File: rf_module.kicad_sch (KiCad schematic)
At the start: 23 parts, among them J5 RF Antenna, Q1 BC848, Q2 BC848, U7 SIM800C-DS

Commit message: Dual SIM version
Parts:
- removed Q1, Q2: BC848, Package_TO_SOT_SMD:SOT-23, symbol Transistor_BJT:BC848
- removed R15, R19: 4.7k, Resistor_SMD:R_0805_2012Metric_Pad1.20x1.40mm_HandSolder, symbol Device:R
- removed R16, R20: 47k, Resistor_SMD:R_0805_2012Metric_Pad1.20x1.40mm_HandSolder, symbol Device:R
- added Q1: MUN5233DW1, Package_TO_SOT_SMD:SOT-363_SC-70-6, symbol symbols:MUN5233DW1
- renumbered R17 to R15, R18 to R16, R21 to R17
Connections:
- net GNDD: now also Q1.1 (E), Q1.4 (E)
- net NETLIGHT: now also Q1.5 (B)
- net STATUS: now also Q1.2 (B)
- net at D6.1 (K): now also Q1.6 (C)
- net at D8.1 (K): now also Q1.3 (C)

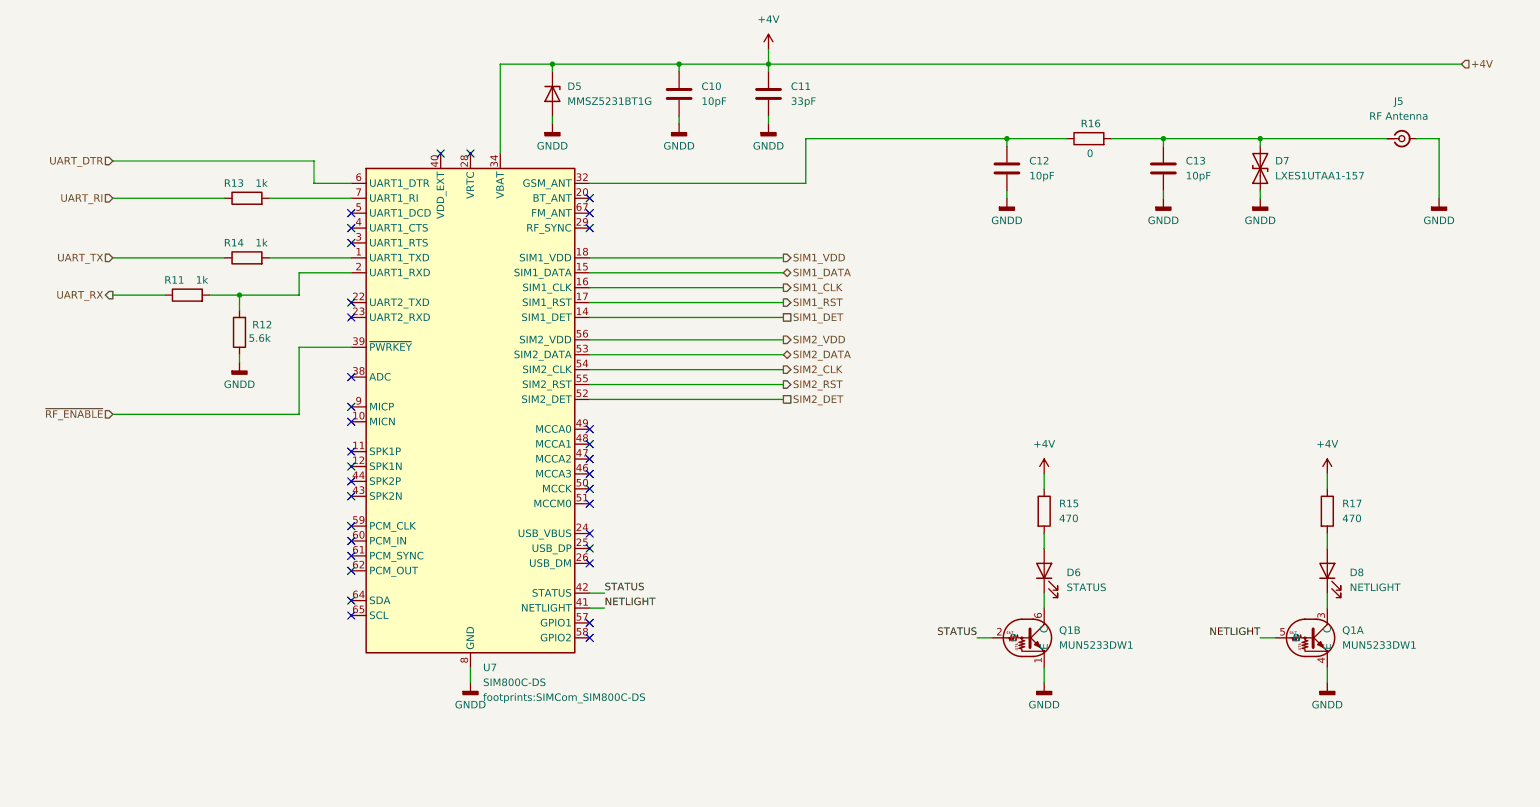
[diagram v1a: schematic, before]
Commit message: Replace SIM800C-DS with A7682E
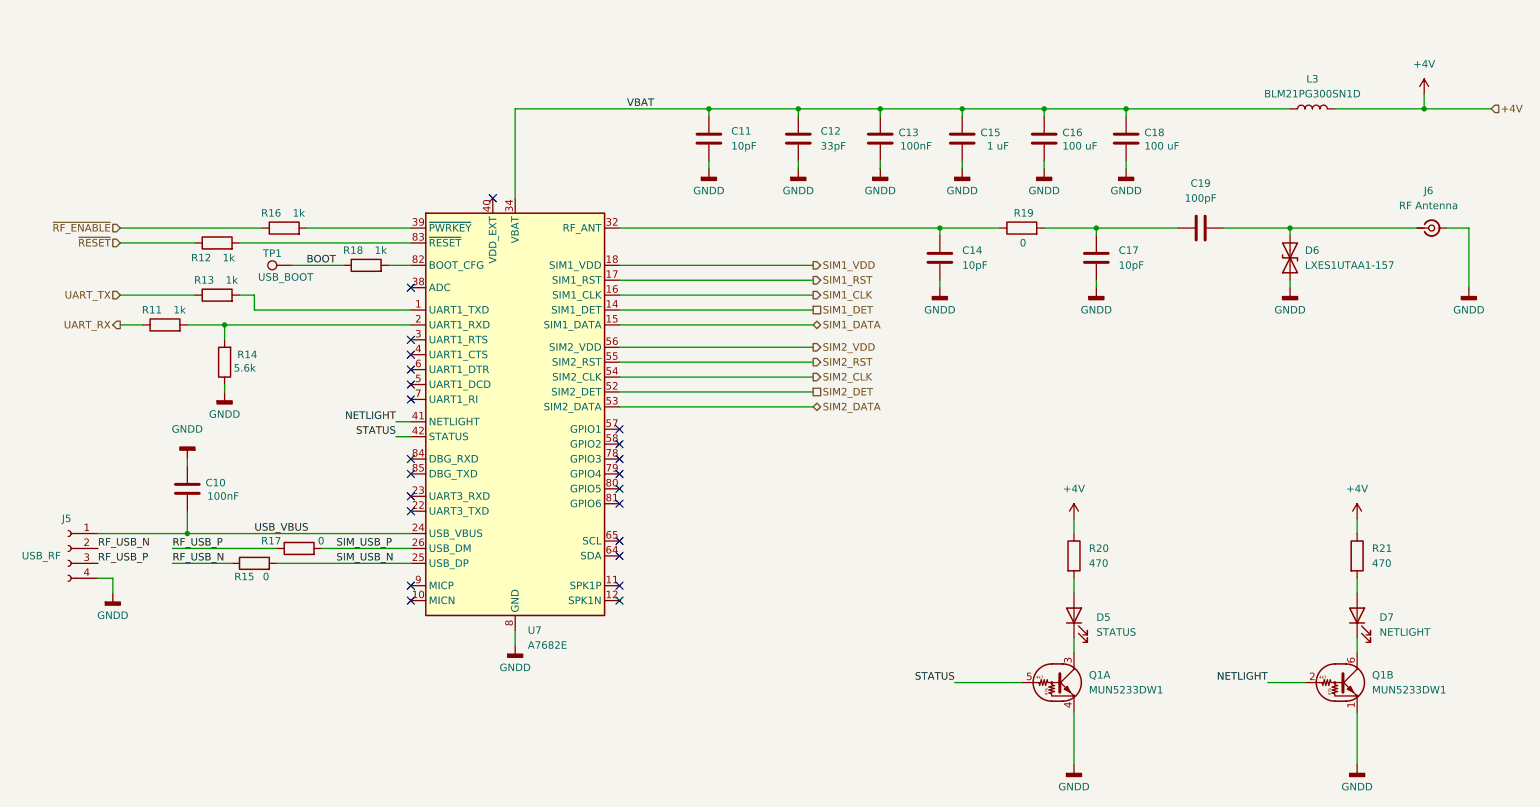
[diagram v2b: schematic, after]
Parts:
- removed D5: MMSZ5231BT1G, Diode_SMD:D_SOD-123, symbol Device:D_Zener
- removed D6: STATUS, LED_SMD:LED_0805_2012Metric_Pad1.15x1.40mm_HandSolder, symbol Device:LED
- removed D7: LXES1UTAA1-157, Diode_SMD:D_01005_0402Metric_Pad0.57x0.30mm_HandSolder, symbol Device:D_TVS
- removed D8: NETLIGHT, LED_SMD:LED_0805_2012Metric_Pad1.15x1.40mm_HandSolder, symbol Device:LED
- removed J5: RF Antenna, footprints:SMA_HJ-SMA405, symbol symbols:SMA_conn_HJ-SMA405
- removed U7: SIM800C-DS, footprints:SIMCom_SIM800C-DS, symbol symbols:SIM800C-DS
- added C14, C17: 10pF, Capacitor_SMD:C_0402_1005Metric, symbol Device:C
- added C15: 1 uF, Capacitor_SMD:C_0805_2012Metric_Pad1.18x1.45mm_HandSolder, symbol Device:C
- added C16, C18: 100 uF, Capacitor_SMD:C_1206_3216Metric_Pad1.33x1.80mm_HandSolder, symbol Device:C
- added C19: 100pF, Capacitor_SMD:C_0402_1005Metric, symbol Device:C
- added D5: STATUS, LED_SMD:LED_0805_2012Metric_Pad1.15x1.40mm_HandSolder, symbol Device:LED
- added D6: LXES1UTAA1-157, Diode_SMD:D_01005_0402Metric, symbol Device:D_TVS
- added D7: NETLIGHT, LED_SMD:LED_0805_2012Metric_Pad1.15x1.40mm_HandSolder, symbol Device:LED
- added J5: USB_RF, Connector_PinHeader_1.27mm:PinHeader_1x04_P1.27mm_Vertical, symbol Connector:Conn_01x04_Socket
- added J6: RF Antenna, footprints:SMA_HJ-SMA405, symbol symbols:SMA_conn_HJ-SMA405
- added L3: BLM21PG300SN1D, Inductor_SMD:L_0805_2012Metric, symbol Device:L
- added R18: 1k, Resistor_SMD:R_0805_2012Metric_Pad1.20x1.40mm_HandSolder, symbol Device:R
- added R19: 0, Resistor_SMD:R_0402_1005Metric, symbol Device:R
- added R20, R21: 470, Resistor_SMD:R_0805_2012Metric_Pad1.20x1.40mm_HandSolder, symbol Device:R
- added TP1: USB_BOOT, TestPoint:TestPoint_Pad_D2.0mm, symbol Connector:TestPoint
- added U7: A7682E, footprints:SIMCom_A7682E_LGA-85, symbol symbols:A7682E
- C10: value 10pF -> 100nF; MPN CC0805JRNPO9BN100 -> CC0805KRX7R8BB104
- C11: value 33pF -> 10pF; MPN CC0805JRNPO9BN330 -> CC0805JRNPO9BN100
- C12: value 10pF -> 33pF; footprint Capacitor_SMD:C_0603_1608Metric_Pad1.08x0.95mm_HandSolder -> Capacitor_SMD:C_0805_2012Metric_Pad1.18x1.45mm_HandSolder; MPN CC0603JRNPO9BN100 -> CC0805JRNPO9BN330
- C13: value 10pF -> 100nF; footprint Capacitor_SMD:C_0603_1608Metric_Pad1.08x0.95mm_HandSolder -> Capacitor_SMD:C_0805_2012Metric_Pad1.18x1.45mm_HandSolder; MPN CC0603JRNPO9BN100 -> CC0805KRX7R8BB104
- Q1: MPN (none) -> MMUN2133LT1G
- R12: value 5.6k -> 1k; MPN RC0805JR-075K6L -> RC0805JR-071KL
- R14: value 1k -> 5.6k; MPN RC0805JR-071KL -> RC0805JR-075K6L
- R15, R17: value 470 -> 0; footprint Resistor_SMD:R_0805_2012Metric_Pad1.20x1.40mm_HandSolder -> Resistor_SMD:R_0402_1005Metric; MPN RC0805JR-07470RL -> RC0402JR-070RL
- R16: value 0 -> 1k; footprint Resistor_SMD:R_0603_1608Metric_Pad0.98x0.95mm_HandSolder -> Resistor_SMD:R_0603_1608Metric; MPN RC0603JR-070RL -> RC0603JR-071KL
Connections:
- net UART_RI is gone; now on net UART_TX: R13.1
- net +4V: now also L3.2, R20.1, R21.1; no longer C10.2, C11.2, R15.1, R17.1
- net GNDD: now also C10.2, R14.1, C14.1, C15.1, C16.1, C17.1, C18.1, D6.1 (A1), J5.4 (Pin_4), J6.2 (Ext), U7.13 (GND), U7.19 (GND), U7.21 (GND), U7.27 (GND), U7.30 (GND), U7.31 (GND), U7.33 (GND), U7.36 (GND), U7.37 (GND), U7.45 (GND), U7.63 (GND), U7.66 (GND), U7.67 (GND), U7.69 (GND), U7.70 (GND), U7.71 (GND), U7.72 (GND), U7.73 (GND), U7.74 (GND), U7.75 (GND), U7.76 (GND), U7.77 (GND), U7.8 (GND); no longer C10.1, R12.1
- net NETLIGHT: now also Q1.2 (B), U7.41 (NETLIGHT); no longer Q1.5 (B)
- net SIM1_CLK: now also U7.16 (SIM1_CLK)
- net SIM1_DATA: now also U7.15 (SIM1_DATA)
- net SIM1_DET: now also U7.14 (SIM1_DET)
- net SIM1_RST: now also U7.17 (SIM1_RST)
- net SIM1_VDD: now also U7.18 (SIM1_VDD)
- net SIM2_CLK: now also U7.54 (SIM2_CLK)
- net SIM2_DATA: now also U7.53 (SIM2_DATA)
- net SIM2_DET: now also U7.52 (SIM2_DET)
- net SIM2_RST: now also U7.55 (SIM2_RST)
- net SIM2_VDD: now also U7.56 (SIM2_VDD)
- net STATUS: now also Q1.5 (B), U7.42 (STATUS); no longer Q1.2 (B)
- net UART_TX: no longer R14.1
- net ~{RF_ENABLE}: now also R16.1
- net at R11.2: now also R14.2, U7.2 (UART1_RXD); no longer R12.2
- net at R16.2: now also U7.39 (~{PWRKEY}); no longer C13.2
- net at Q1.6 (C): now also D7.1 (K)
- net SIM_USB_N: now reaches R15.2
- net SIM_USB_N: now also U7.25 (USB_DP)
- net VBAT: now reaches C12.2
- net VBAT: now also C11.2, C13.2, C15.2, C16.2, C18.2, L3.1, U7.34 (VBAT), U7.35 (VBAT); no longer R16.1
- net at R13.2: now also U7.1 (UART1_TXD)
- net at Q1.3 (C): now also D5.1 (K)
- net SIM_USB_P: now reaches R17.2
- net SIM_USB_P: now also U7.26 (USB_DM)
- new net: D7.2 (A), R21.2
- new net: U7.20 (NC), U7.28 (NC), U7.29 (NC), U7.43 (NC), U7.44 (NC), U7.46 (NC), U7.47 (NC), U7.48 (NC), U7.49 (NC), U7.50 (NC), U7.51 (NC), U7.59 (NC), U7.60 (NC), U7.61 (NC), U7.62 (NC), U7.68 (NC)
- new net: C14.2, R19.1, U7.32 (RF_ANT)
- new net: R18.2, U7.82 (BOOT_CFG)
- new net: R12.2, U7.83 (~{RESET})
- new net: C17.2, C19.2, R19.2
- new net: C19.1, D6.2 (A2), J6.1 (In)
- new net: D5.2 (A), R20.2
- new net BOOT: R18.1, TP1.1
- new net RF_USB_N: J5.2 (Pin_2), R15.1
- new net RF_USB_P: J5.3 (Pin_3), R17.1
- new net USB_VBUS: C10.1, J5.1 (Pin_1), U7.24 (USB_VBUS)
- new net ~{RESET}: R12.1
- no-connect marks 34 -> 23

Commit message: USB connector inversion fix
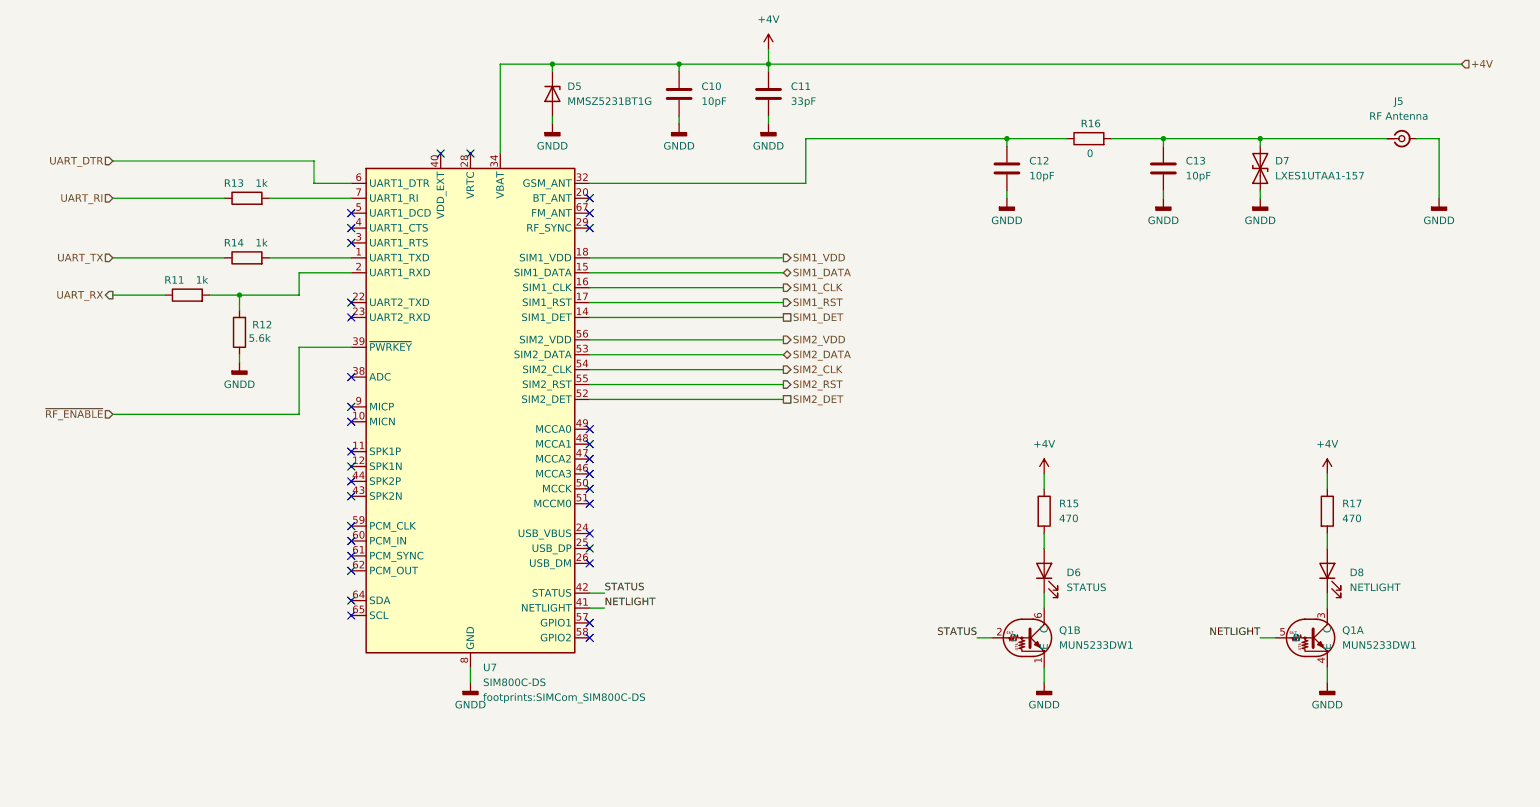
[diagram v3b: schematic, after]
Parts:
- removed C14, C17: 10pF, Capacitor_SMD:C_0402_1005Metric, symbol Device:C
- removed C15: 1 uF, Capacitor_SMD:C_0805_2012Metric_Pad1.18x1.45mm_HandSolder, symbol Device:C
- removed C16, C18: 100 uF, Capacitor_SMD:C_1206_3216Metric_Pad1.33x1.80mm_HandSolder, symbol Device:C
- removed C19: 100pF, Capacitor_SMD:C_0402_1005Metric, symbol Device:C
- removed D5: STATUS, LED_SMD:LED_0805_2012Metric_Pad1.15x1.40mm_HandSolder, symbol Device:LED
- removed D6: LXES1UTAA1-157, Diode_SMD:D_01005_0402Metric, symbol Device:D_TVS
- removed D7: NETLIGHT, LED_SMD:LED_0805_2012Metric_Pad1.15x1.40mm_HandSolder, symbol Device:LED
- removed J5: USB_RF, Connector_PinHeader_1.27mm:PinHeader_1x04_P1.27mm_Vertical, symbol Connector:Conn_01x04_Socket
- removed J6: RF Antenna, footprints:SMA_HJ-SMA405, symbol symbols:SMA_conn_HJ-SMA405
- removed L3: BLM21PG300SN1D, Inductor_SMD:L_0805_2012Metric, symbol Device:L
- removed R18: 1k, Resistor_SMD:R_0805_2012Metric_Pad1.20x1.40mm_HandSolder, symbol Device:R
- removed R19: 0, Resistor_SMD:R_0402_1005Metric, symbol Device:R
- removed R20, R21: 470, Resistor_SMD:R_0805_2012Metric_Pad1.20x1.40mm_HandSolder, symbol Device:R
- removed TP1: USB_BOOT, TestPoint:TestPoint_Pad_D2.0mm, symbol Connector:TestPoint
- removed U7: A7682E, footprints:SIMCom_A7682E_LGA-85, symbol symbols:A7682E
- added D5: MMSZ5231BT1G, Diode_SMD:D_SOD-123, symbol Device:D_Zener
- added D6: STATUS, LED_SMD:LED_0805_2012Metric_Pad1.15x1.40mm_HandSolder, symbol Device:LED
- added D7: LXES1UTAA1-157, Diode_SMD:D_01005_0402Metric_Pad0.57x0.30mm_HandSolder, symbol Device:D_TVS
- added D8: NETLIGHT, LED_SMD:LED_0805_2012Metric_Pad1.15x1.40mm_HandSolder, symbol Device:LED
- added J5: RF Antenna, footprints:SMA_HJ-SMA405, symbol symbols:SMA_conn_HJ-SMA405
- added U7: SIM800C-DS, footprints:SIMCom_SIM800C-DS, symbol symbols:SIM800C-DS
- C10: value 100nF -> 10pF; MPN CC0805KRX7R8BB104 -> CC0805JRNPO9BN100
- C11: value 10pF -> 33pF; MPN CC0805JRNPO9BN100 -> CC0805JRNPO9BN330
- C12: value 33pF -> 10pF; footprint Capacitor_SMD:C_0805_2012Metric_Pad1.18x1.45mm_HandSolder -> Capacitor_SMD:C_0603_1608Metric_Pad1.08x0.95mm_HandSolder; MPN CC0805JRNPO9BN330 -> CC0603JRNPO9BN100
- C13: value 100nF -> 10pF; footprint Capacitor_SMD:C_0805_2012Metric_Pad1.18x1.45mm_HandSolder -> Capacitor_SMD:C_0603_1608Metric_Pad1.08x0.95mm_HandSolder; MPN CC0805KRX7R8BB104 -> CC0603JRNPO9BN100
- Q1: MPN MMUN2133LT1G -> (none)
- R12: value 1k -> 5.6k; MPN RC0805JR-071KL -> RC0805JR-075K6L
- R14: value 5.6k -> 1k; MPN RC0805JR-075K6L -> RC0805JR-071KL
- R15, R17: value 0 -> 470; footprint Resistor_SMD:R_0402_1005Metric -> Resistor_SMD:R_0805_2012Metric_Pad1.20x1.40mm_HandSolder; MPN RC0402JR-070RL -> RC0805JR-07470RL
- R16: value 1k -> 0; footprint Resistor_SMD:R_0603_1608Metric -> Resistor_SMD:R_0603_1608Metric_Pad0.98x0.95mm_HandSolder; MPN RC0603JR-071KL -> RC0603JR-070RL
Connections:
- net RF_USB_N is gone; now on net +4V: R15.1
- net RF_USB_P is gone; now on net +4V: R17.1
- net USB_VBUS is gone; now on net GNDD: C10.1
- net ~{RESET} is gone; now on net GNDD: R12.1
- net +4V: now also C10.2, C11.2, D5.1 (K), U7.34 (VBAT), U7.35 (VBAT)
- net GNDD: now also D5.2 (A), D7.1 (A1), J5.2 (Ext), U7.13 (GND), U7.19 (GND), U7.21 (GND), U7.27 (GND), U7.30 (GND), U7.31 (GND), U7.33 (GND), U7.36 (GND), U7.37 (GND), U7.45 (GND), U7.63 (GND), U7.66 (GND), U7.68 (GND), U7.69 (GND), U7.70 (GND), U7.71 (GND), U7.72 (GND), U7.73 (GND), U7.74 (GND), U7.75 (GND), U7.76 (GND), U7.77 (GND), U7.8 (GND); no longer C10.2, R14.1
- net NETLIGHT: now also Q1.5 (B), U7.41 (NETLIGHT); no longer Q1.2 (B)
- net SIM1_CLK: now also U7.16 (SIM1_CLK)
- net SIM1_DATA: now also U7.15 (SIM1_DATA)
- net SIM1_DET: now also U7.14 (SIM1_DET)
- net SIM1_RST: now also U7.17 (SIM1_RST)
- net SIM1_VDD: now also U7.18 (SIM1_VDD)
- net SIM2_CLK: now also U7.54 (SIM2_CLK)
- net SIM2_DATA: now also U7.53 (SIM2_DATA)
- net SIM2_DET: now also U7.52 (SIM2_DET)
- net SIM2_RST: now also U7.55 (SIM2_RST)
- net SIM2_VDD: now also U7.56 (SIM2_VDD)
- net STATUS: now also Q1.2 (B), U7.42 (STATUS); no longer Q1.5 (B)
- net UART_TX: now also R14.1; no longer R13.1
- net ~{RF_ENABLE}: now also U7.39 (~{PWRKEY}); no longer R16.1
- net at Q1.6 (C): now also D6.1 (K)
- net at R13.2: now also U7.7 (UART1_RI)
- net at R11.2: now also R12.2, U7.2 (UART1_RXD); no longer R14.2
- net at R16.2: now also C13.2, D7.2 (A2), J5.1 (In)
- net at Q1.3 (C): now also D8.1 (K)
- net SIM_USB_N: no longer names the net of R15.2
- net SIM_USB_N: now also D6.2 (A)
- net SIM_USB_P: no longer names the net of R17.2
- net SIM_USB_P: now also D8.2 (A)
- removed net VBAT: C11.2, C12.2, C13.2
- new net: R14.2, U7.1 (UART1_TXD)
- new net: C12.2, R16.1, U7.32 (GSM_ANT)
- new net UART_DTR: U7.6 (UART1_DTR)
- new net UART_RI: R13.1
- no-connect marks 23 -> 34
